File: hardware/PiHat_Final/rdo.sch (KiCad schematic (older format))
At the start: 16 parts

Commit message: Added more to the Schematic.
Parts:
- C14, C15: renamed from C?; footprint (none) -> Capacitors_SMD:C_0805
- Y1: renamed from Y?; footprint (none) -> Crystals:Crystal_SMD_HC49-SD
- gave numbers to parts that had none: 13
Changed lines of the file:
@@
 $EndDescr
 $Comp
-L Si4464 U?
+L Si4464 U4
 U 1 1 58E9F2F9
 P 8600 3450
-F 0 "U?" H 9000 3000 60  0000 C CNN
+F 0 "U4" H 9000 3000 60  0000 C CNN
 F 1 "Si4464" H 9050 3950 60  0000 C CNN
 F 2 "Housings_DFN_QFN:QFN-20-1EP_4x4mm_Pitch0.5mm" H 8600 3450 60  0001 C CNN
@@
 	8600 2400 8600 2800
 $Comp
-L GND #PWR?
+L GND #PWR27
 U 1 1 58E9F2FA
 P 8500 2500
-F 0 "#PWR?" H 8500 2250 50  0001 C CNN
+F 0 "#PWR27" H 8500 2250 50  0001 C CNN
 F 1 "GND" H 8500 2350 50  0000 C CNN
 F 2 "" H 8500 2500 50  0000 C CNN
@@
 NoConn ~ 8500 4050
 $Comp
-L +3V3 #PWR?
+L +3V3 #PWR26
 U 1 1 58E9F2FD
 P 8000 4050
-F 0 "#PWR?" H 8000 3900 50  0001 C CNN
+F 0 "#PWR26" H 8000 3900 50  0001 C CNN
 F 1 "+3V3" H 8000 4190 50  0000 C CNN
 F 2 "" H 8000 4050 50  0000 C CNN
@@
 	7950 3550 7650 3550
 $Comp
-L C C?
+L C C11
 U 1 1 58E9F2FE
 P 7500 3550
-F 0 "C?" H 7525 3650 50  0000 L CNN
+F 0 "C11" H 7525 3650 50  0000 L CNN
 F 1 "4.7pF" H 7525 3450 50  0000 L CNN
 F 2 "Capacitors_SMD:C_0805" H 7538 3400 50  0001 C CNN
@@
 	7350 3550 7250 3550
 $Comp
-L L_Small L?
+L L_Small L5
 U 1 1 58E9F2FF
 P 7750 3850
-F 0 "L?" H 7780 3890 50  0000 L CNN
+F 0 "L5" H 7780 3890 50  0000 L CNN
 F 1 "36nH" H 7780 3810 50  0000 L CNN
 F 2 "Resistors_SMD:R_0805" H 7750 3850 50  0001 C CNN
@@
 Connection ~ 8000 4150
 $Comp
-L L_Small L?
+L L_Small L3
 U 1 1 58E9F300
 P 7150 3550
-F 0 "L?" H 7180 3590 50  0000 L CNN
+F 0 "L3" H 7180 3590 50  0000 L CNN
 F 1 "27nH" H 7180 3510 50  0000 L CNN
 F 2 "Resistors_SMD:R_0805" H 7150 3550 50  0001 C CNN
@@
 Connection ~ 6950 3550
 $Comp
-L C C?
+L C C8
 U 1 1 58E9F301
 P 6950 3800
-F 0 "C?" H 6975 3900 50  0000 L CNN
+F 0 "C8" H 6975 3900 50  0000 L CNN
 F 1 "12pF" H 6975 3700 50  0000 L CNN
 F 2 "Capacitors_SMD:C_0805" H 6988 3650 50  0001 C CNN
@@
 $EndComp
 $Comp
-L L_Small L?
+L L_Small L2
 U 1 1 58E9F302
 P 6750 3550
-F 0 "L?" H 6780 3590 50  0000 L CNN
+F 0 "L2" H 6780 3590 50  0000 L CNN
 F 1 "11nH" H 6780 3510 50  0000 L CNN
 F 2 "Resistors_SMD:R_0805" H 6750 3550 50  0001 C CNN
@@
 	6450 3550 6650 3550
 $Comp
-L C C?
+L C C7
 U 1 1 58E9F303
 P 6550 3800
-F 0 "C?" H 6575 3900 50  0000 L CNN
+F 0 "C7" H 6575 3900 50  0000 L CNN
 F 1 "5.1pF" H 6575 3700 50  0000 L CNN
 F 2 "Capacitors_SMD:C_0805" H 6588 3650 50  0001 C CNN
@@
 	6550 3950 6550 4050
 $Comp
-L GND #PWR?
+L GND #PWR23
 U 1 1 58E9F304
 P 6550 4050
-F 0 "#PWR?" H 6550 3800 50  0001 C CNN
+F 0 "#PWR23" H 6550 3800 50  0001 C CNN
 F 1 "GND" H 6550 3900 50  0000 C CNN
 F 2 "" H 6550 4050 50  0000 C CNN
@@
 	6950 3950 6950 4050
 $Comp
-L GND #PWR?
+L GND #PWR24
 U 1 1 58E9F305
 P 6950 4050
-F 0 "#PWR?" H 6950 3800 50  0001 C CNN
+F 0 "#PWR24" H 6950 3800 50  0001 C CNN
 F 1 "GND" H 6950 3900 50  0000 C CNN
 F 2 "" H 6950 4050 50  0000 C CNN
@@
 $EndComp
 $Comp
-L C C?
+L C C6
 U 1 1 58E9F306
 P 6300 3550
-F 0 "C?" H 6325 3650 50  0000 L CNN
+F 0 "C6" H 6325 3650 50  0000 L CNN
 F 1 "4.7pF" H 6325 3450 50  0000 L CNN
 F 2 "Capacitors_SMD:C_0805" H 6338 3400 50  0001 C CNN
@@
 	7650 3350 7150 3350
 $Comp
-L L_Small L?
+L L_Small L4
 U 1 1 58E9F307
 P 7250 3150
-F 0 "L?" H 7280 3190 50  0000 L CNN
+F 0 "L4" H 7280 3190 50  0000 L CNN
 F 1 "36nH" H 7280 3110 50  0000 L CNN
 F 2 "Resistors_SMD:R_0805" H 7250 3150 50  0001 C CNN
@@
 	7250 3350 7250 3250
 $Comp
-L C C?
+L C C10
 U 1 1 58E9F308
 P 7250 2700
-F 0 "C?" H 7275 2800 50  0000 L CNN
+F 0 "C10" H 7275 2800 50  0000 L CNN
 F 1 "5.6pF" H 7275 2600 50  0000 L CNN
 F 2 "Capacitors_SMD:C_0805" H 7288 2550 50  0001 C CNN
@@
 Connection ~ 7250 2950
 $Comp
-L C C?
+L C C9
 U 1 1 58E9F309
 P 7000 3350
-F 0 "C?" H 7025 3450 50  0000 L CNN
+F 0 "C9" H 7025 3450 50  0000 L CNN
 F 1 "4.7pF" H 7025 3250 50  0000 L CNN
 F 2 "Capacitors_SMD:C_0805" H 7038 3200 50  0001 C CNN
@@
 	7250 2350 7250 2550
 $Comp
-L GND #PWR?
+L GND #PWR25
 U 1 1 58E9F30A
 P 7050 2450
-F 0 "#PWR?" H 7050 2200 50  0001 C CNN
+F 0 "#PWR25" H 7050 2200 50  0001 C CNN
 F 1 "GND" H 7050 2300 50  0000 C CNN
 F 2 "" H 7050 2450 50  0000 C CNN
@@
 A
 $Comp
-L C C?
+L C C13
 U 1 1 58E9F33E
 P 8650 4500
-F 0 "C?" H 8675 4600 50  0000 L CNN
+F 0 "C13" H 8675 4600 50  0000 L CNN
 F 1 "10nF" H 8675 4400 50  0000 L CNN
 F 2 "Capacitors_SMD:C_0805" H 8688 4350 50  0001 C CNN
@@
 $EndComp
 $Comp
-L C C?
+L C C12
 U 1 1 58E9F33F
 P 8350 4500
-F 0 "C?" H 8375 4600 50  0000 L CNN
+F 0 "C12" H 8375 4600 50  0000 L CNN
 F 1 "10nF" H 8375 4400 50  0000 L CNN
 F 2 "Capacitors_SMD:C_0805" H 8388 4350 50  0001 C CNN
@@
 $EndComp
 $Comp
-L GND #PWR?
+L GND #PWR28
 U 1 1 58E9F340
 P 8500 4850
-F 0 "#PWR?" H 8500 4600 50  0001 C CNN
+F 0 "#PWR28" H 8500 4600 50  0001 C CNN
 F 1 "GND" H 8500 4700 50  0000 C CNN
 F 2 "" H 8500 4850 50  0000 C CNN
@@
 $EndComp
 $Comp
-L Crystal Y?
+L Crystal Y1
 U 1 1 58E9FBD6
 P 8900 2050
-F 0 "Y?" H 8900 2200 50  0000 C CNN
+F 0 "Y1" H 8900 2200 50  0000 C CNN
 F 1 "30MHz" H 8900 1900 50  0000 C CNN
-F 2 "" H 8900 2050 50  0000 C CNN
+F 2 "Crystals:Crystal_SMD_HC49-SD" H 8900 2050 50  0001 C CNN
 F 3 "" H 8900 2050 50  0000 C CNN
 	1    8900 2050
@@
 Connection ~ 8900 2300
 $Comp
-L C C?
+L C C15
 U 1 1 58E9FE46
 P 9250 2300
-F 0 "C?" H 9275 2400 50  0000 L CNN
+F 0 "C15" H 9275 2400 50  0000 L CNN
 F 1 "20pF" H 9275 2200 50  0000 L CNN
-F 2 "" H 9288 2150 50  0000 C CNN
+F 2 "Capacitors_SMD:C_0805" H 9288 2150 50  0001 C CNN
 F 3 "" H 9250 2300 50  0000 C CNN
 	1    9250 2300
@@
 $EndComp
 $Comp
-L C C?
+L C C14
 U 1 1 58E9FE9C
 P 9250 1800
-F 0 "C?" H 9275 1900 50  0000 L CNN
+F 0 "C14" H 9275 1900 50  0000 L CNN
 F 1 "20pF" H 9275 1700 50  0000 L CNN
-F 2 "" H 9288 1650 50  0000 C CNN
+F 2 "Capacitors_SMD:C_0805" H 9288 1650 50  0001 C CNN
 F 3 "" H 9250 1800 50  0000 C CNN
 	1    9250 1800
@@
 Connection ~ 9500 2300
 $Comp
-L GND #PWR?
+L GND #PWR29
 U 1 1 58E9FFE6
 P 9500 2400
-F 0 "#PWR?" H 9500 2150 50  0001 C CNN
+F 0 "#PWR29" H 9500 2150 50  0001 C CNN
 F 1 "GND" H 9500 2250 50  0000 C CNN
 F 2 "" H 9500 2400 50  0000 C CNN

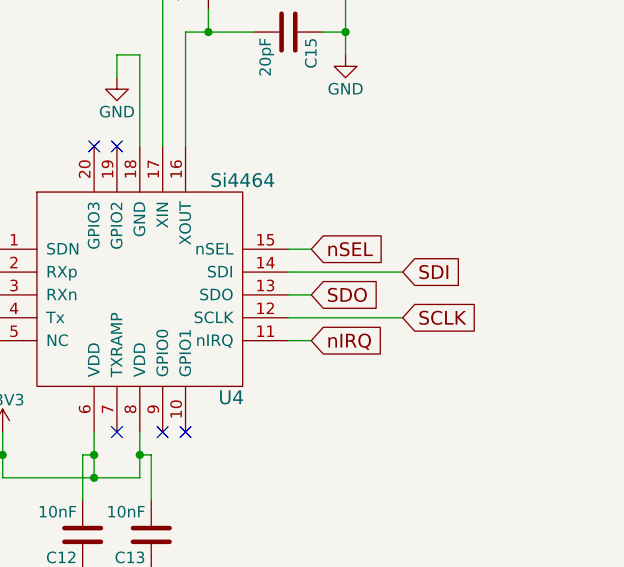
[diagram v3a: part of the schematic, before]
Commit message: Transciever wiring & Power Distribution Changes, modified footprint for Edge SMA, swapped TX/RX on ANTSEL
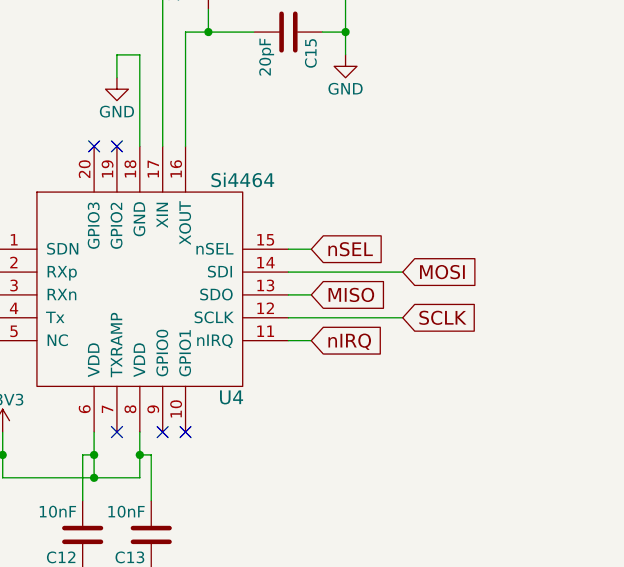
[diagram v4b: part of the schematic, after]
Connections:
- net SDI renamed MOSI
- net SDO renamed MISO
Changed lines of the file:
@@
 	8600 2400 8600 2800
 $Comp
-L GND #PWR023
+L GND #PWR027
 U 1 1 58E9F2FA
 P 8500 2500
-F 0 "#PWR023" H 8500 2250 50  0001 C CNN
+F 0 "#PWR027" H 8500 2250 50  0001 C CNN
 F 1 "GND" H 8500 2350 50  0000 C CNN
 F 2 "" H 8500 2500 50  0000 C CNN
@@
 NoConn ~ 8500 4050
 $Comp
-L +3V3 #PWR024
+L +3V3 #PWR028
 U 1 1 58E9F2FD
 P 8000 4050
-F 0 "#PWR024" H 8000 3900 50  0001 C CNN
+F 0 "#PWR028" H 8000 3900 50  0001 C CNN
 F 1 "+3V3" H 8000 4190 50  0000 C CNN
 F 2 "" H 8000 4050 50  0000 C CNN
@@
 nSEL
 Text GLabel 9350 3450 2    60   Input ~ 0
-SDO
+MISO
 Wire Wire Line
 	9250 3350 9750 3350
@@
 	9250 3550 9750 3550
 Text GLabel 9750 3350 2    60   Input ~ 0
-SDI
+MOSI
 Text GLabel 9750 3550 2    60   Input ~ 0
 SCLK
@@
 	6550 3950 6550 4050
 $Comp
-L GND #PWR025
+L GND #PWR029
 U 1 1 58E9F304
 P 6550 4050
-F 0 "#PWR025" H 6550 3800 50  0001 C CNN
+F 0 "#PWR029" H 6550 3800 50  0001 C CNN
 F 1 "GND" H 6550 3900 50  0000 C CNN
 F 2 "" H 6550 4050 50  0000 C CNN
@@
 	6950 3950 6950 4050
 $Comp
-L GND #PWR026
+L GND #PWR030
 U 1 1 58E9F305
 P 6950 4050
-F 0 "#PWR026" H 6950 3800 50  0001 C CNN
+F 0 "#PWR030" H 6950 3800 50  0001 C CNN
 F 1 "GND" H 6950 3900 50  0000 C CNN
 F 2 "" H 6950 4050 50  0000 C CNN
@@
 	7250 2350 7250 2550
 $Comp
-L GND #PWR027
+L GND #PWR031
 U 1 1 58E9F30A
 P 7050 2450
-F 0 "#PWR027" H 7050 2200 50  0001 C CNN
+F 0 "#PWR031" H 7050 2200 50  0001 C CNN
 F 1 "GND" H 7050 2300 50  0000 C CNN
 F 2 "" H 7050 2450 50  0000 C CNN
@@
 $EndComp
 $Comp
-L GND #PWR028
+L GND #PWR032
 U 1 1 58E9F340
 P 8500 4850
-F 0 "#PWR028" H 8500 4600 50  0001 C CNN
+F 0 "#PWR032" H 8500 4600 50  0001 C CNN
 F 1 "GND" H 8500 4700 50  0000 C CNN
 F 2 "" H 8500 4850 50  0000 C CNN
@@
 Connection ~ 9500 2300
 $Comp
-L GND #PWR029
+L GND #PWR033
 U 1 1 58E9FFE6
 P 9500 2400
-F 0 "#PWR029" H 9500 2150 50  0001 C CNN
+F 0 "#PWR033" H 9500 2150 50  0001 C CNN
 F 1 "GND" H 9500 2250 50  0000 C CNN
 F 2 "" H 9500 2400 50  0000 C CNN
